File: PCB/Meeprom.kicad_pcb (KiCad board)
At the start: 2 copper layers, 38 x 16.6 mm, 3 parts, among them J1 Molex 78805 socket with 27C25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, U1 28C256 / FM18W08

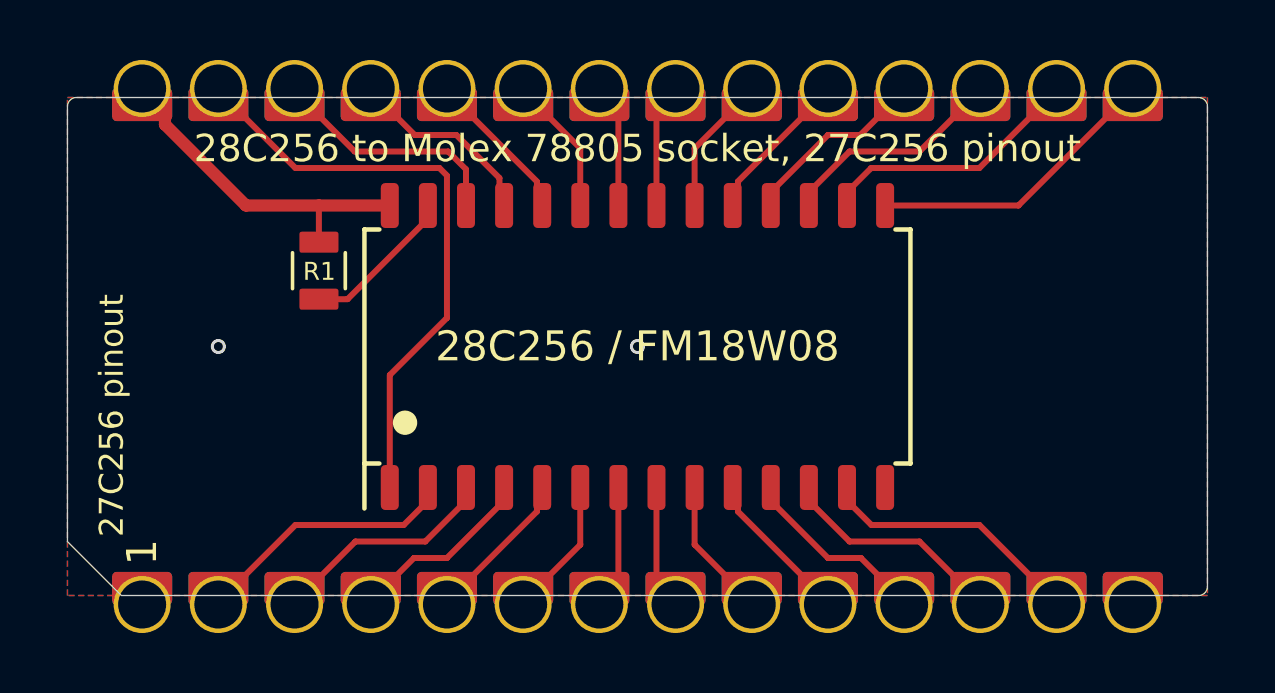
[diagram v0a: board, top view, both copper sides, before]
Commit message: add caps & fiducials, remove dead shapeways links
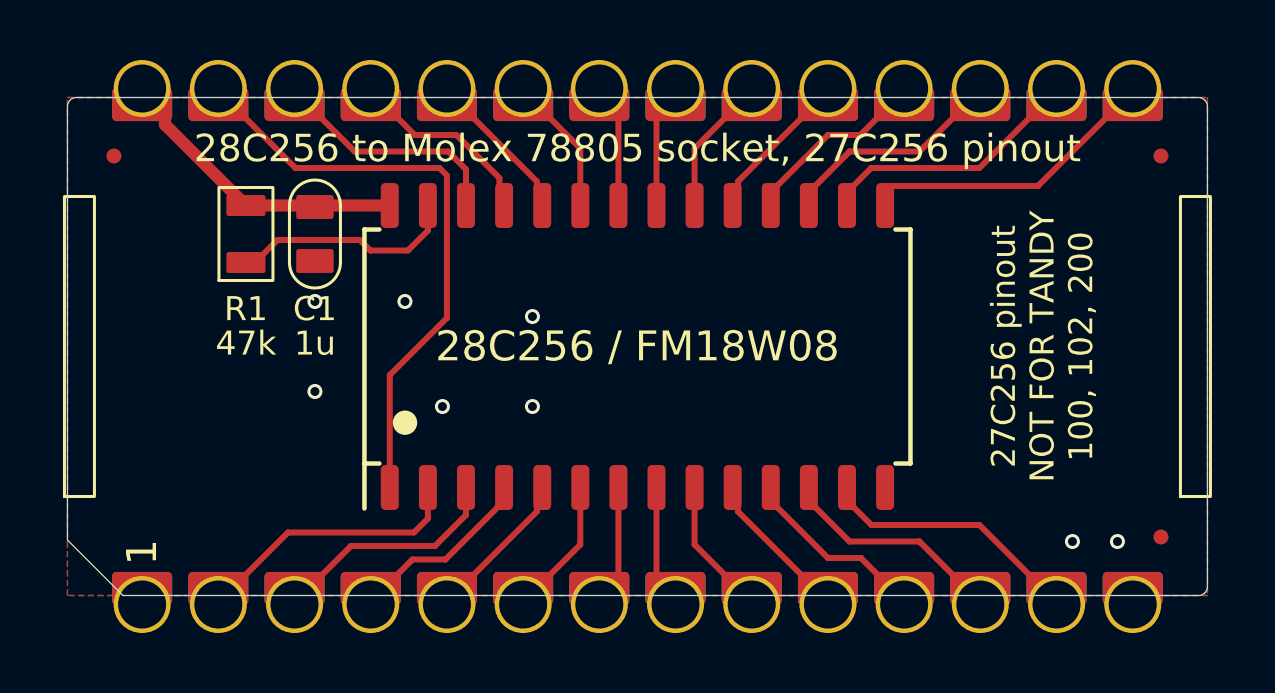
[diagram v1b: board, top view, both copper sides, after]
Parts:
- added C1: 1u, 000_LOCAL:C_0805, F.Cu at (136.5, 95.4)
- added N1: Molex78802_PCB_28_Carrier, 000_LOCAL:Molex78802_PCB_28_Carrier, F.Cu at (147.2, 99.2)
- added REF**: Fiducial_0.5mm_Mask1mm, 000_LOCAL:Fiducial_0.5mm_Mask1mm, F.Cu at (164.7, 105.5)
- added REF**: Fiducial_0.5mm_Mask1mm, 000_LOCAL:Fiducial_0.5mm_Mask1mm, F.Cu at (164.7, 92.8)
- added REF**: Fiducial_0.5mm_Mask1mm, 000_LOCAL:Fiducial_0.5mm_Mask1mm, F.Cu at (129.8, 92.8)
- moved R1 2.72 mm to (134.2, 95.4)
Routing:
- net /~{WE}: track 5.19 -> 7.63 mm
- net VCC: track 11.4 -> 10.2 mm
- net GND: vias 2 -> 8
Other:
- board text added: "27C256 pinout NOT FOR TANDY 100, 102, 200"
- board text added: "R1: 10k - 100k C1: 0.1u - 1u Carrier: ${d7c0df55-2d7f-416a-bbbd-010a17333805:VALUE}"
- board text removed: "27C256 pinout"
- board text removed: "NOT for TRS-80/TANDY Model 100, 102, 200"
- board text removed: "R1: ${00000000-0000-0000-0000-00005d22c129:VALUE} Use Carrier: Molex78802_PCB_28 v004"
